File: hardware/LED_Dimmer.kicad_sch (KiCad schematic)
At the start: 14 parts, among them J1 Kyocera - Poke-Home 1x04, J2 1x16, 0.05" Pitch Vertical He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, J3 Kyocera - Poke-Home 1x04, J4 1x16, 0.05" Pitch Vertical He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, Q1 2N7002K-7, Q2 2N7002K-7, Q3 2N7002K-7, U1 BGM220P, U2 L78L33A

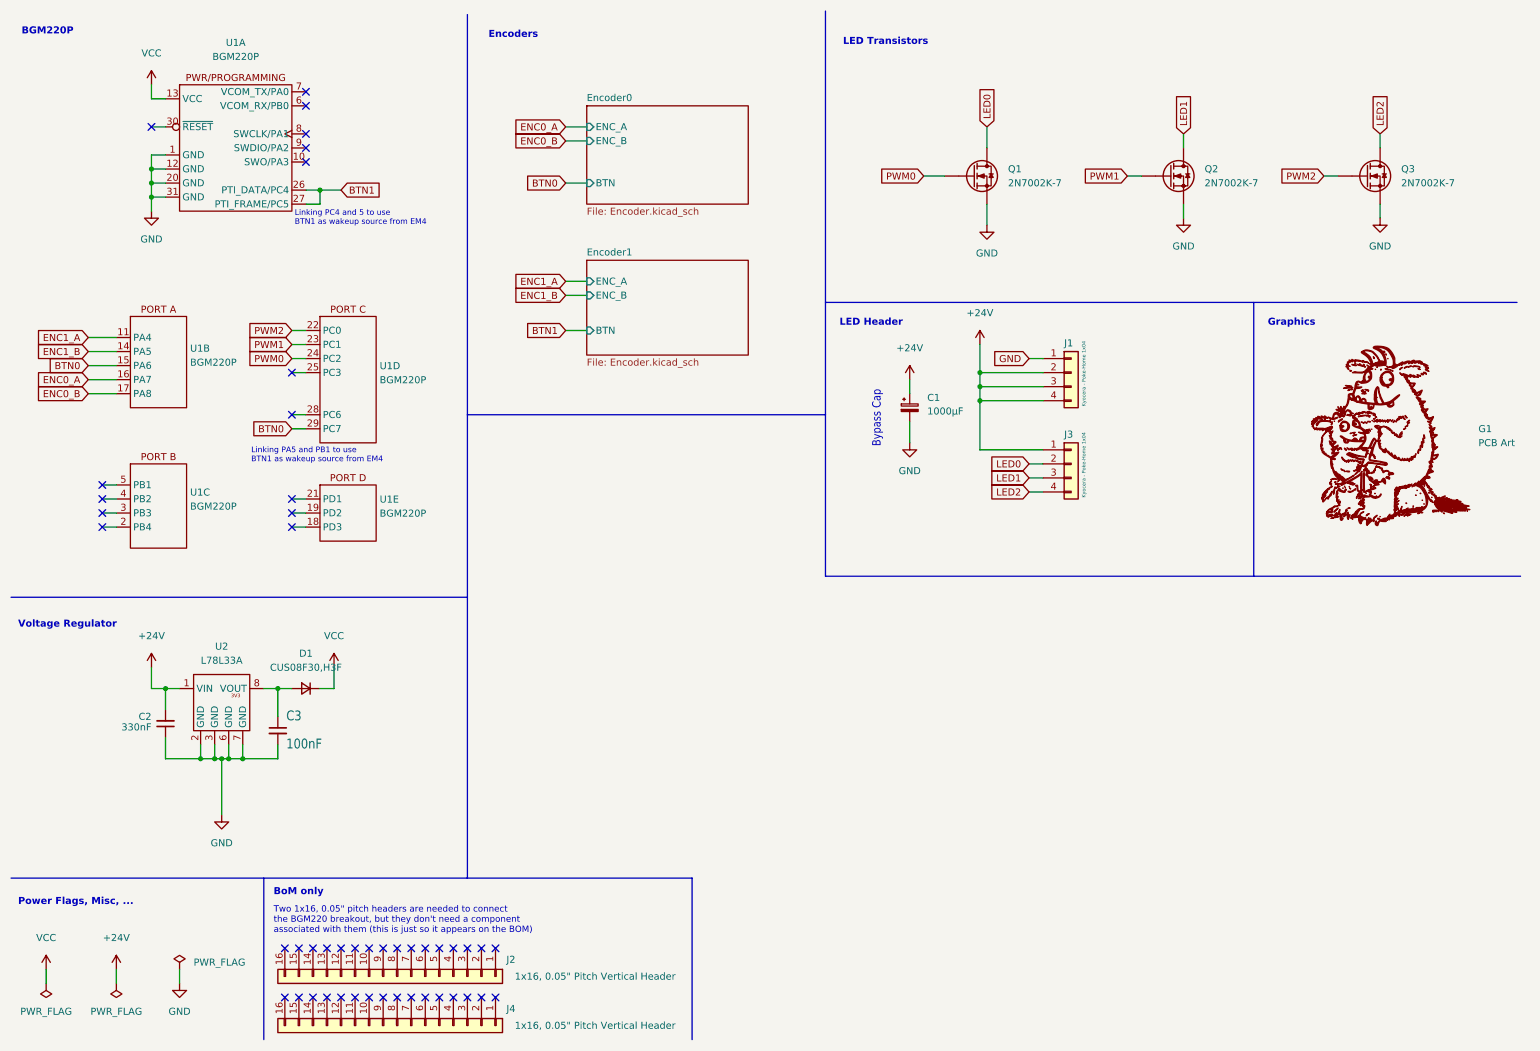
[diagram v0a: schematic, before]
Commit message: Added Kyocera Connector
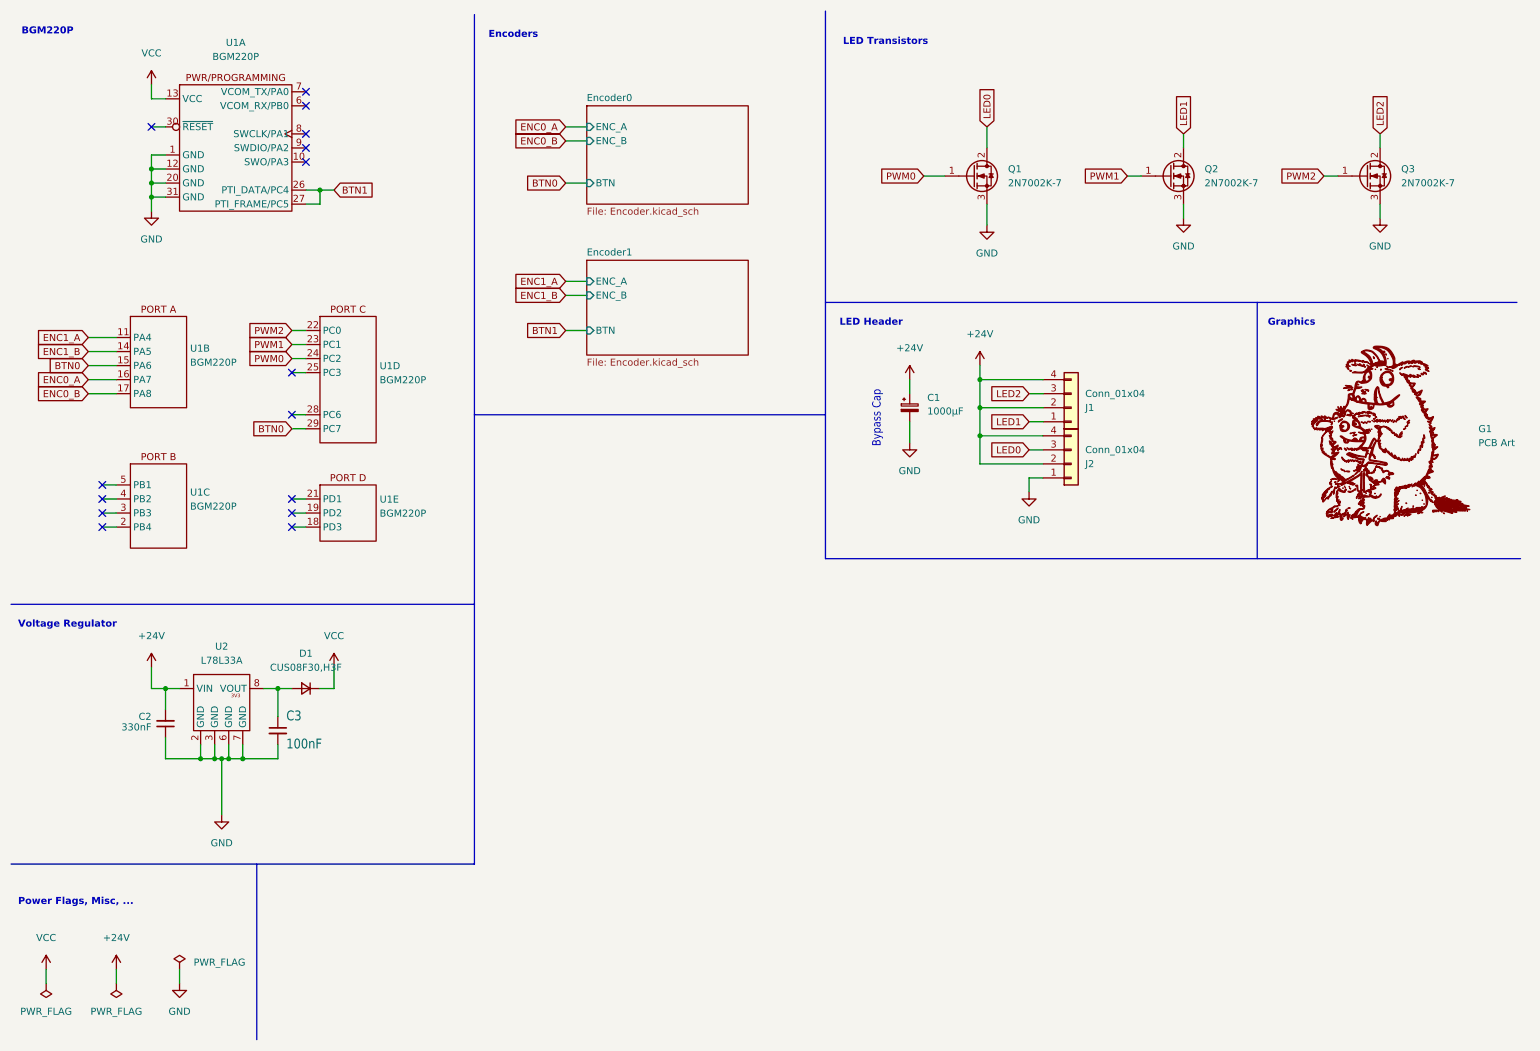
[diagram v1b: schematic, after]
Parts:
- removed J2, J4: 1x16, 0.05" Pitch Vertical Header, symbol Connector_Generic:Conn_01x16
- removed J3: Kyocera - Poke-Home 1x04, Gruffalo_Dimmer:Connector - Kyocera - Poke-Home 1x04 – Standard Horizontal 18-26 AWG, symbol Connector_Generic:Conn_01x04
- added J2: Conn_01x04, Gruffalo_Dimmer:Connector - Kyocera - Poke-Home 1x04 – Standard Horizontal 18-26 AWG, symbol Connector_Generic:Conn_01x04
- G1: Digikey PN - -> (none); Farnell PN - -> (none); MPN - -> (none); Manufacturer - -> (none)
- J1: value Kyocera - Poke-Home 1x04 -> Conn_01x04; Comments Kyocera - Poke-Home 1x04 – Standard Horizontal 18-26 AWG -> Poke-Home Wire To Board Connector, 18-26AWG, 4 Ways; Farnell PN 1891140 -> 4243865; MPN 009276004021906 -> 9276004021906; Vrating (none) -> 300V / 6A
- Q1, Q2, Q3: symbol Device:Q_NMOS -> Transistor_FET:Q_NMOS_GDS
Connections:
- net +24V: now also J2.2 (Pin_2), J2.4 (Pin_4); no longer J1.3 (Pin_3)
- net GND: now also Q1.3 (S), Q2.3 (S), Q3.3 (S), J2.1 (Pin_1); no longer J1.1 (Pin_1), Q1.S, Q2.S, Q3.S
- net LED0: now also Q1.2 (D), J2.3 (Pin_3); no longer Q1.D
- net LED1: now also J1.1 (Pin_1), Q2.2 (D); no longer Q2.D
- net LED2: now also J1.3 (Pin_3), Q3.2 (D); no longer Q3.D
- net PWM0: now also Q1.1 (G); no longer Q1.G
- net PWM1: now also Q2.1 (G); no longer Q2.G
- net PWM2: now also Q3.1 (G); no longer Q3.G
- no-connect marks 47 -> 15
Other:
- note removed: "BoM only"
- note removed: "Linking PA5 and PB1 to use BTN1 as wakeup source from EM4"
- note removed: "Linking PC4 and 5 to use BTN1 as wakeup source from EM4"
- note removed: "Two 1x16, 0.05" pitch headers are needed to connect the BGM220 breakout, but they don't need a component associated with them (this is just so it appears on the BOM)"

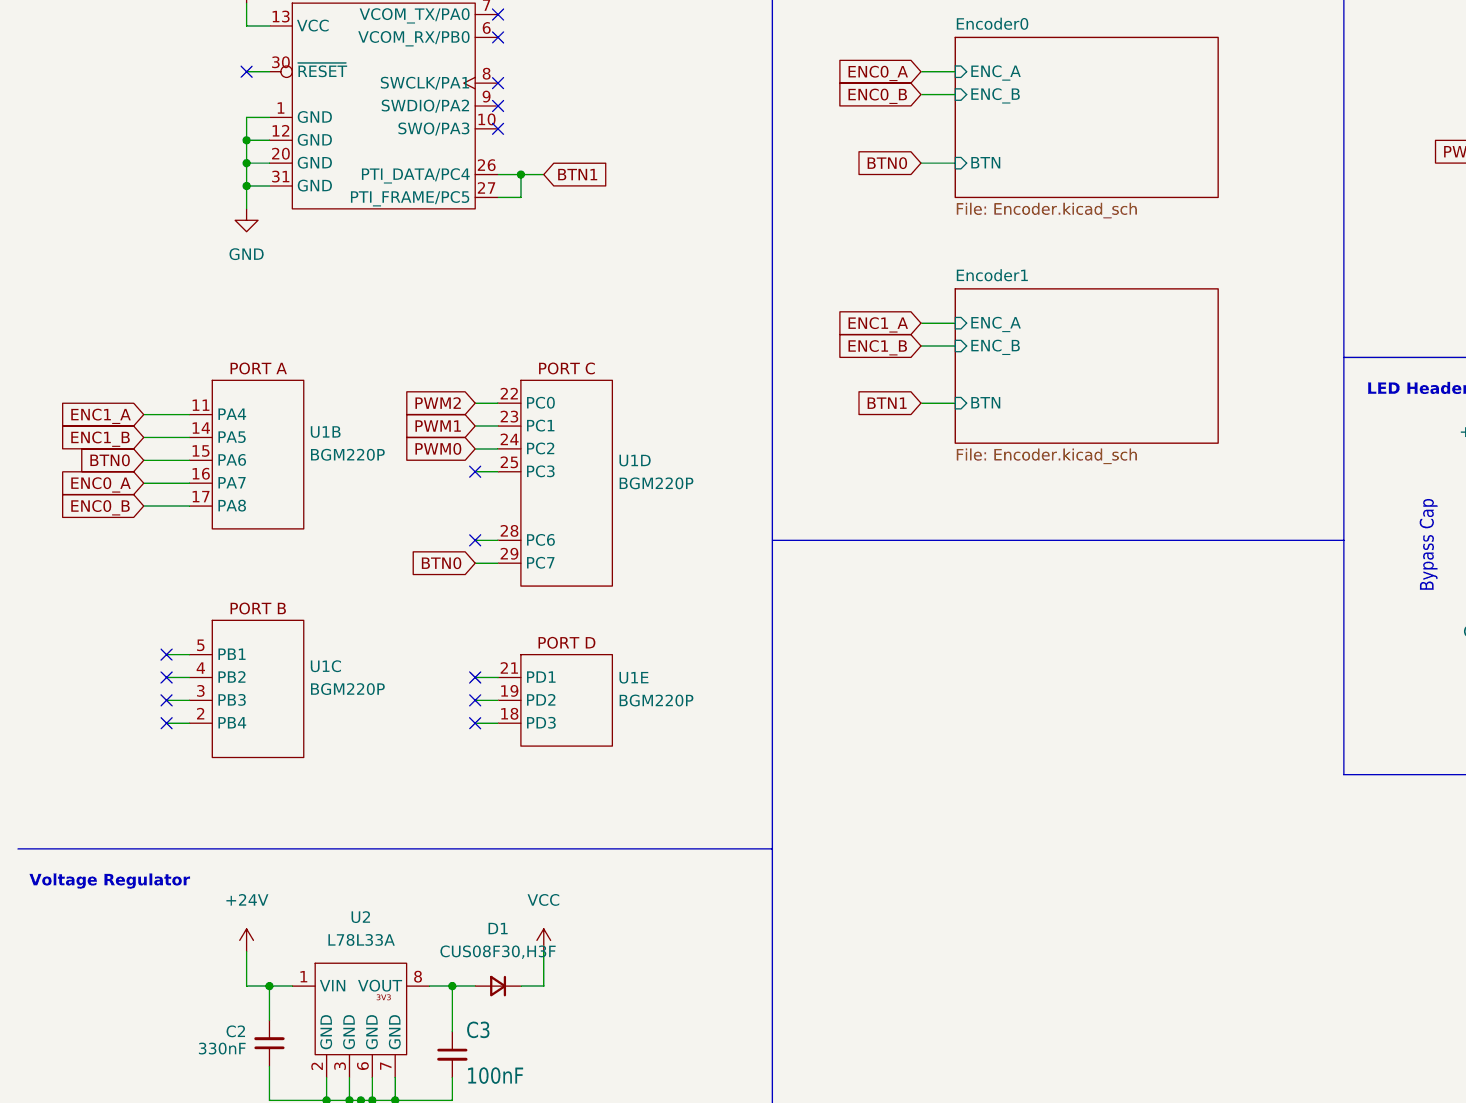
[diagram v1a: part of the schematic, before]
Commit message: Added LED Indicators
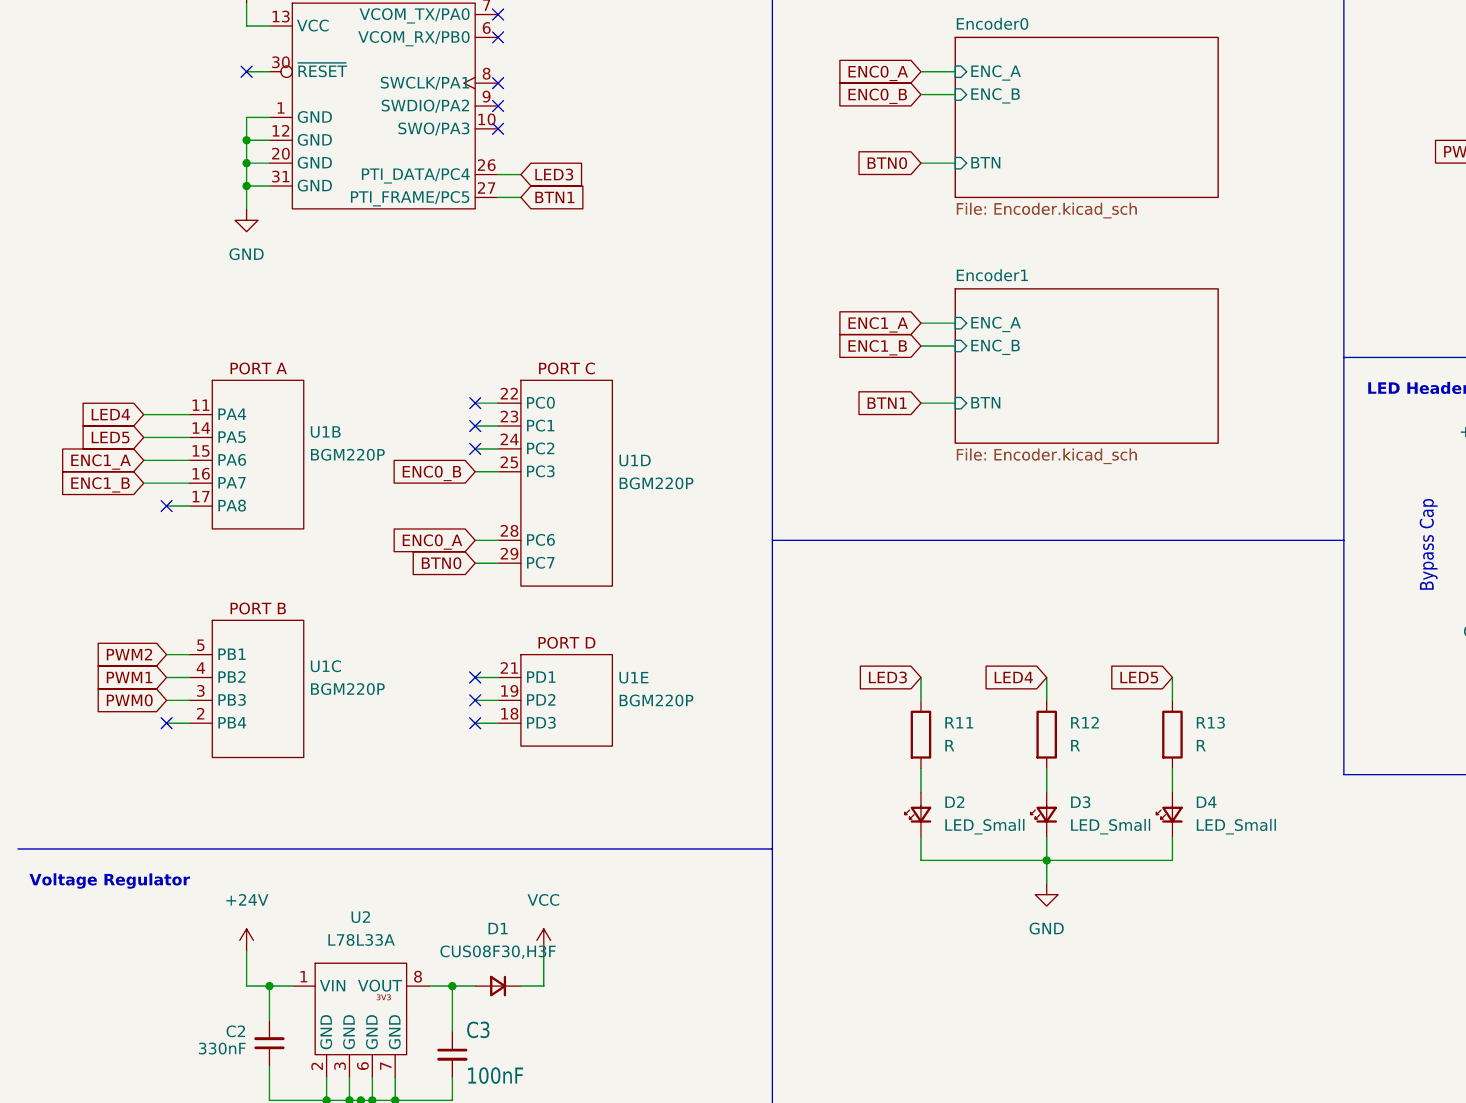
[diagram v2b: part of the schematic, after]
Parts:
- added D2, D3, D4: LED_Small, Gruffalo_Dimmer:0603-1.6x0.8mm-LED_Handsolder, symbol Device:LED_Small
- added R11, R12, R13: R, Gruffalo_Dimmer:0805-R_Handsolder, symbol Device:R
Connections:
- net BTN0: no longer U1.15 (PA6)
- net BTN1: no longer U1.26 (PTI_DATA/PC4)
- net ENC0_A: now also U1.28 (PC6); no longer U1.16 (PA7)
- net ENC0_B: now also U1.25 (PC3); no longer U1.17 (PA8)
- net ENC1_A: now also U1.15 (PA6); no longer U1.11 (PA4)
- net ENC1_B: now also U1.16 (PA7); no longer U1.14 (PA5)
- net GND: now also D2.1 (K), D3.1 (K), D4.1 (K)
- net PWM0: now also U1.3 (PB3); no longer U1.24 (PC2)
- net PWM1: now also U1.4 (PB2); no longer U1.23 (PC1)
- net PWM2: now also U1.5 (PB1); no longer U1.22 (PC0)
- new net: D3.2 (A), R12.2
- new net: D2.2 (A), R11.2
- new net: D4.2 (A), R13.2
- new net LED3: R11.1, U1.26 (PTI_DATA/PC4)
- new net LED4: R12.1, U1.11 (PA4)
- new net LED5: R13.1, U1.14 (PA5)
- no-connect marks 15 -> 14

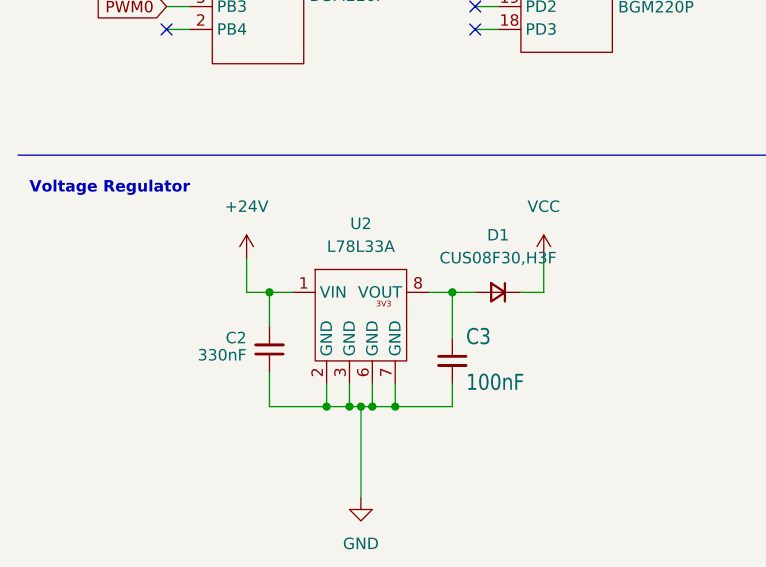
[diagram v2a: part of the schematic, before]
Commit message: Regulator pinout was wrong! Also decoupling cap was not decoupling
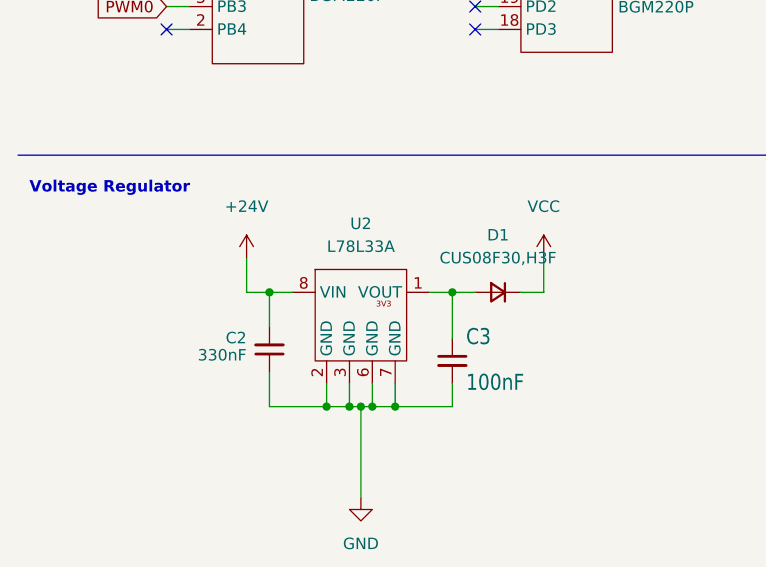
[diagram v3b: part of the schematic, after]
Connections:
- net +24V: now also U2.8 (VIN); no longer U2.1 (VIN)
- net at C3.1, D1.2 (A): now also U2.1 (VOUT); no longer U2.8 (VOUT)
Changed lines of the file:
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@@
 			)
 		)
-		(property "Sim.Enable" ""
-			(at 127 106.68 0)
-			(effects
-				(font
-					(size 1.27 1.27)
-				)
-				(hide yes)
-			)
-		)
 		(pin "1"
 		)
@@
 			)
 		)
-		(property "Sim.Enable" ""
-			(at 40.64 140.97 0)
-			(effects
-				(font
-					(size 1.27 1.27)
-				)
-				(hide yes)
-			)
-		)
 		(pin "1"
 		)
@@
 			)
 		)
-		(property "Sim.Enable" ""
-			(at 222.25 41.91 0)
-			(effects
-				(font
-					(size 1.27 1.27)
-				)
-				(hide yes)
-			)
-		)
 		(pin "1"
 		)
@@
 			)
 		)
-		(property "Sim.Enable" ""
-			(at 127 115.57 90)
-			(effects
-				(font
-					(size 1.27 1.27)
-				)
-				(hide yes)
-			)
-		)
 		(pin "1"
 		)
@@
 			)
 		)
-		(property "Sim.Enable" ""
-			(at 53.34 36.83 0)
-			(effects
-				(font
-					(size 1.27 1.27)
-				)
-				(hide yes)
-			)
-		)
 		(pin "1"
 		)
@@
 			)
 		)
-		(property "Sim.Enable" ""
-			(at 204.47 83.82 0)
-			(effects
-				(font
-					(size 1.27 1.27)
-				)
-				(hide yes)
-			)
-		)
 		(pin "2"
 		)
@@
 		)
 		(instances
-			(project ""
+			(project "LED_Dimmer"
 				(path "/682943ce-d527-4ae2-be9e-cc5eaf184b84"
 					(reference "J1")
@@
 			)
 		)
-		(property "Sim.Enable" ""
-			(at 73.66 102.87 0)
-			(effects
-				(font
-					(size 1.27 1.27)
-				)
-				(hide yes)
-			)
-		)
 		(pin "1"
 		)
@@
 			)
 		)
-		(property "Sim.Enable" ""
-			(at 113.03 115.57 90)
-			(effects
-				(font
-					(size 1.27 1.27)
-				)
-				(hide yes)
-			)
-		)
 		(pin "1"
 		)
@@
 		)
 		(instances
-			(project ""
+			(project "LED_Dimmer"
 				(path "/682943ce-d527-4ae2-be9e-cc5eaf184b84"
 					(reference "D2")
@@
 			)
 		)
-		(property "Sim.Enable" ""
-			(at 60.96 142.24 0)
-			(effects
-				(font
-					(size 1.27 1.27)
-				)
-				(hide yes)
-			)
-		)
 		(pin "1"
 		)
@@
 			)
 		)
-		(property "Sim.Enable" ""
-			(at 140.97 115.57 90)
-			(effects
-				(font
-					(size 1.27 1.27)
-				)
-				(hide yes)
-			)
-		)
 		(pin "1"
 		)
@@
 			)
 		)
-		(property "Sim.Enable" ""
-			(at 186.69 41.91 0)
-			(effects
-				(font
-					(size 1.27 1.27)
-				)
-				(hide yes)
-			)
-		)
 		(pin "1"
 		)
@@
 			)
 		)
-		(property "Sim.Enable" ""
-			(at 66.04 134.62 0)
-			(effects
-				(font
-					(size 1.27 1.27)
-				)
-				(hide yes)
-			)
-		)
 		(pin "1"
 		)
@@
 			)
 		)
-		(property "Sim.Enable" ""
-			(at 50.8 137.16 0)
-			(effects
-				(font
-					(size 1.27 1.27)
-				)
-				(hide yes)
-			)
-		)
 		(pin "1"
 		)
@@
 			)
 		)
-		(property "Sim.Enable" ""
-			(at 73.66 78.74 0)
-			(effects
-				(font
-					(size 1.27 1.27)
-				)
-				(hide yes)
-			)
-		)
 		(pin "1"
 		)
@@
 			)
 		)
-		(property "Sim.Enable" ""
-			(at 113.03 106.68 0)
-			(effects
-				(font
-					(size 1.27 1.27)
-				)
-				(hide yes)
-			)
-		)
 		(pin "1"
 		)
@@
 		)
 		(instances
-			(project ""
+			(project "LED_Dimmer"
 				(path "/682943ce-d527-4ae2-be9e-cc5eaf184b84"
 					(reference "R11")
@@
 			)
 		)
-		(property "Sim.Enable" ""
-			(at 257.81 41.91 0)
-			(effects
-				(font
-					(size 1.27 1.27)
-				)
-				(hide yes)
-			)
-		)
 		(pin "1"
 		)
@@
 			)
 		)
-		(property "Sim.Enable" ""
-			(at 39.37 76.2 0)
-			(effects
-				(font
-					(size 1.27 1.27)
-				)
-				(hide yes)
-			)
-		)
 		(pin "1"
 		)
@@
 			)
 		)
-		(property "Sim.Enable" ""
-			(at 39.37 101.6 0)
-			(effects
-				(font
-					(size 1.27 1.27)
-				)
-				(hide yes)
-			)
-		)
 		(pin "1"
 		)
@@
 			)
 		)
-		(property "Sim.Enable" ""
-			(at 262.255 88.9 0)
-			(effects
-				(font
-					(size 1.27 1.27)
-				)
-				(hide yes)
-			)
-		)
 		(instances
 			(project "LED_Dimmer"
@@
 			)
 		)
-		(property "Sim.Enable" ""
-			(at 175.26 83.82 0)
-			(effects
-				(font
-					(size 1.27 1.27)
-				)
-				(hide yes)
-			)
-		)
 		(pin "1"
 		)
@@
 			)
 		)
-		(property "Sim.Enable" ""
-			(at 140.97 106.68 0)
-			(effects
-				(font
-					(size 1.27 1.27)
-				)
-				(hide yes)
-			)
-		)
 		(pin "1"
 		)
@@
 			(at 204.47 93.98 0)
 			(effects
-				(font
-					(size 1.27 1.27)
-				)
-				(hide yes)
-			)
-		)
-		(property "Sim.Enable" ""
-			(at 204.47 93.98 0)
-			(effects
